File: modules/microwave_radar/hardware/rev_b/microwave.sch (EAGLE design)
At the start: 55 parts, among them J1 MODULE_GENERIC, J2 TC2030-JLINK-L, U1 SAM4LC8AA, U2 TLV62130, U3 MSGEQ7, U4 HB100, U5 OP284E_SEPARATE

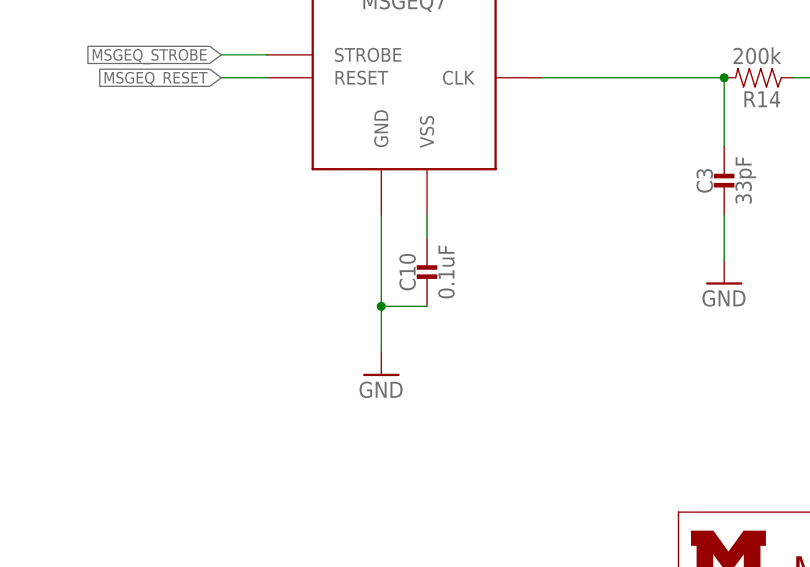
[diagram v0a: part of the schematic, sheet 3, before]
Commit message: Fix MSGEQ7 swapped pins!!!
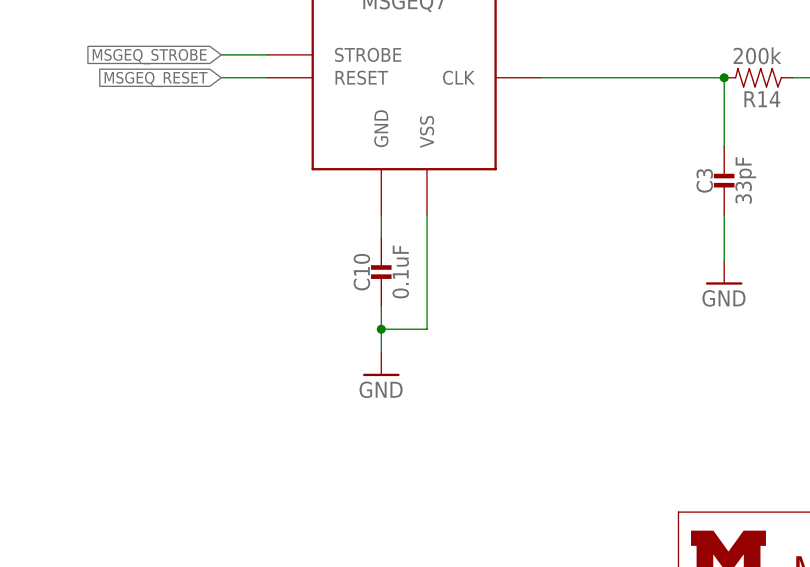
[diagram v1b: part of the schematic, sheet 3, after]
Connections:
- net GND: now also U3.VSS; no longer U3.GND
- net N$7: now also U3.GND; no longer U3.VSS
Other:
- moved on the sheet: C10
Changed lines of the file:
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@@
 <?xml version="1.0" encoding="utf-8"?>
 <!DOCTYPE eagle SYSTEM "eagle.dtd">
-<eagle version="7.7.0">
+<eagle version="6.6.0">
 <drawing>
 <settings>
@@
 <attribute name="DIGIKEY" x="86.36" y="91.44" size="1.778" layer="96" rot="R90" display="off"/>
 </instance>
-<instance part="C10" gate="G$1" x="99.06" y="38.1">
-<attribute name="DIGIKEY" x="99.06" y="38.1" size="1.778" layer="96" display="off"/>
+<instance part="C10" gate="G$1" x="93.98" y="38.1">
+<attribute name="DIGIKEY" x="93.98" y="38.1" size="1.778" layer="96" display="off"/>
 </instance>
 <instance part="C3" gate="G$1" x="132.08" y="48.26">
@@
 <segment>
 <pinref part="GND8" gate="1" pin="GND"/>
-<wire x1="99.06" y1="33.02" x2="93.98" y2="33.02" width="0.1524" layer="91"/>
-<wire x1="93.98" y1="33.02" x2="93.98" y2="27.94" width="0.1524" layer="91"/>
-<pinref part="U3" gate="G$1" pin="GND"/>
-<wire x1="93.98" y1="33.02" x2="93.98" y2="43.18" width="0.1524" layer="91"/>
-<junction x="93.98" y="33.02"/>
+<wire x1="93.98" y1="33.02" x2="93.98" y2="30.48" width="0.1524" layer="91"/>
 <pinref part="C10" gate="G$1" pin="2"/>
+<pinref part="U3" gate="G$1" pin="VSS"/>
+<wire x1="93.98" y1="30.48" x2="93.98" y2="27.94" width="0.1524" layer="91"/>
+<wire x1="99.06" y1="43.18" x2="99.06" y2="30.48" width="0.1524" layer="91"/>
+<wire x1="99.06" y1="30.48" x2="93.98" y2="30.48" width="0.1524" layer="91"/>
+<junction x="93.98" y="30.48"/>
 </segment>
 <segment>
@@
 </segment>
 </net>
-<net name="N$7" class="0">
-<segment>
-<pinref part="U3" gate="G$1" pin="VSS"/>
-<wire x1="99.06" y1="43.18" x2="99.06" y2="40.64" width="0.1524" layer="91"/>
-<pinref part="C10" gate="G$1" pin="1"/>
-</segment>
-</net>
 <net name="MSGEQ_OUT" class="0">
 <segment>
@@
 </segment>
 </net>
+<net name="N$7" class="0">
+<segment>
+<pinref part="U3" gate="G$1" pin="GND"/>
+<pinref part="C10" gate="G$1" pin="1"/>
+<wire x1="93.98" y1="40.64" x2="93.98" y2="43.18" width="0.1524" layer="91"/>
+</segment>
+</net>

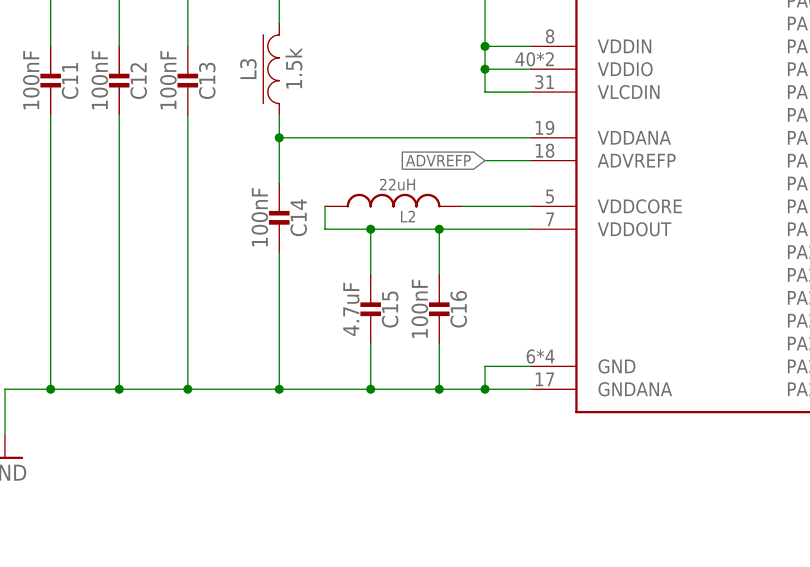
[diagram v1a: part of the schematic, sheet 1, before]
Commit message: moved caps
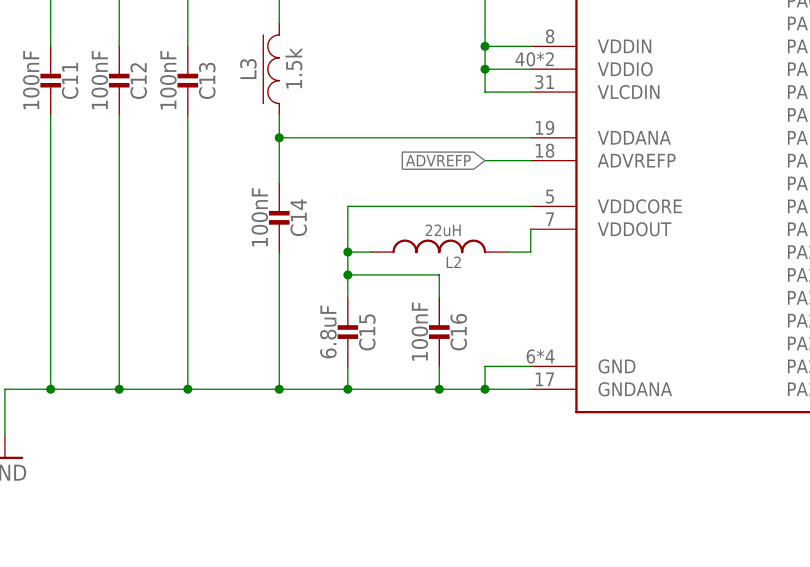
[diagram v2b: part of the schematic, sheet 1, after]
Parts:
- C15: value 4.7uF -> 6.8uF; device passives:CAPACITOR0402_CAP -> passives:CAPACITOR0603_CAP; DIGIKEY 490-13252-1-ND -> 445-7484-1-ND
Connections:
- removed net N$5: L2.2, U1.VDDCORE
- new net N$36: C15.2, C16.2, L2.1, U1.VDDCORE
- net N$6: now also L2.2; no longer C15.2, C16.2, L2.1
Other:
- moved on the sheet: C15, C16, L2

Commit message: added power gates, almost done routing
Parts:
- removed C21: 10uF, passives:CAPACITOR0805_CAP
- removed C22: 22uF, passives:CAPACITOR0603_CAP
- removed C7: 3.3nF, passives:CAPACITOR0402_CAP
- removed C8: 0.1uF, passives:CAPACITOR0402_CAP
- removed L1: 2.2uH, passives:INDUCTORIHL
- removed L3: 1.5k, passives:FERRITE_BEAD0402
- removed LED1: LED0603, leds:LED0603
- removed R1: 1k, passives:RESISTOR0402_RES
- removed R13: 100k, passives:RESISTOR0402_RES
- removed R15: 240k, passives:RESISTOR0402_RES
- removed R17: 750k, passives:RESISTOR0402_RES
- removed U2: TLV62130, chips:TLV62130
- added C28: 10 uF, passives:CAPACITOR0805_CAP
- added C29: 0.1 uF, passives:CAPACITOR0402_CAP
- added C30: 3.3 nF, passives:CAPACITOR0402_CAP
- added C31: 22 uF, passives:CAPACITOR0603_CAP
- added FB1: 1.5k, passives:FERRITE_BEAD0402
- added L5: 2.2 uH, passives:INDUCTORIHL
- added Q1, Q3: SI223DDS, fets:SI223DDS
- added R18, R22, R24: 100k, passives:RESISTOR0402_RES
- added R19, R23: 1k, passives:RESISTOR0402_RES
- added R20: 750k, passives:RESISTOR0402_RES
- added R21: 240k, passives:RESISTOR0402_RES
- added U7: TLV62130, chips:TLV62130
- J1: value MODULE_GENERIC -> MODULE_GENERIC_DEBUG; device signpost:MODULE_GENERIC -> signpost:MODULE_GENERIC_DEBUG
- R11, R12: value 100k -> 1M
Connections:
- net CONTROLLER_XIN renamed XIN
- net CONTROLLER_XOUT renamed XOUT
- removed net CONTROLLER_RESET: J2.!RESET, U1.!RESET
- removed net CONTROLLER_SWDCLK: J2.SWDCLK, R8.1, U1.TCK
- removed net CONTROLLER_SWDIO: J2.SWDIO, R7.1, U1.PA03
- removed net N$16: U1.PA06
- removed net N$20: L1.1, U2.SW
- removed net N$22: U1.PA11
- removed net N$23: R13.1, U2.PG
- removed net N$24: R15.2, R17.1, U2.FB
- removed net N$25: U1.PA12
- removed net N$4: LED1.ANODE, R1.2
- removed net N$8: C7.1, U2.SS/TR
- removed net USART2_RX: JP2.2, U1.PA25
- removed net USART2_TX: JP2.3, U1.PA26
- new net !RESET: J1.DBG_!RESET, J2.!RESET, U1.!RESET
- new net 3V3_GATED: C9.2, Q3.D, R10.2, R14.1, U3.VDD, U5G$2.VCC
- new net DBG_GPIO1: J1.DBG_GPIO1, U1.PA11
- new net DBG_GPIO2: J1.DBG_GPIO2, U1.PA12
- new net DBG_RX: J1.DBG_RX, JP2.2, U1.PA25
- new net DBG_TX: J1.DBG_TX, JP2.3, U1.PA26
- new net N$37: Q1.G, R18.1, R19.2
- new net N$38: Q3.G, R22.1, R23.2
- new net N$42: C30.2, U7.SS/TR
- new net N$43: L5.1, U7.SW
- new net N$44: R24.1, U7.PG
- new net N$45: R20.1, R21.2, U7.FB
- new net N$5: C17.2, Q1.D, U4.5V_1, U4.5V_2
- new net RADAR_POWER_GATE: R19.1, R23.1, U1.PA06
- new net SWDCLK: J1.DBG_SWDCLK, J2.SWDCLK, R8.1, U1.TCK
- new net SWDIO: J1.DBG_SWDIO, J2.SWDIO, R7.1, U1.PA03
- net +3V3: now also C31.2, FB1.P$2, L5.2, Q3.S, R20.2, R22.2, R24.2, U7.VOS; no longer C22.1, C9.2, L1.2, L3.P$2, R1.1, R10.2, R13.2, R14.1, R17.2, U2.VOS, U3.VDD, U5G$2.VCC
- net +5V: now also C28.1, C29.1, Q1.S, R18.2, U7.AVIN, U7.EN, U7.PVIN; no longer C17.2, C21.1, C8.1, U2.AVIN, U2.EN, U2.PVIN, U4.5V_1, U4.5V_2
- net GND: now also C28.2, C29.2, C30.1, C31.1, R21.1, U7.AGND, U7.DEF, U7.FSW, U7.PGND; no longer C21.2, C22.2, C7.2, C8.2, LED1.CATHODE, R15.1, U2.AGND, U2.DEF, U2.FSW, U2.PGND
- net N$13: now also FB1.P$1; no longer L3.P$1

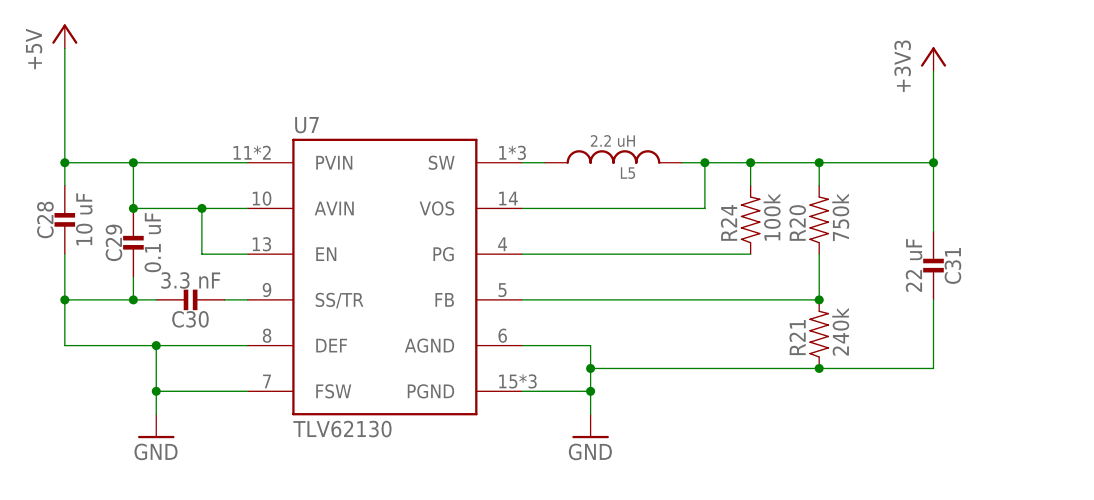
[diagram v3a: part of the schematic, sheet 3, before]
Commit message: changed values to not have space
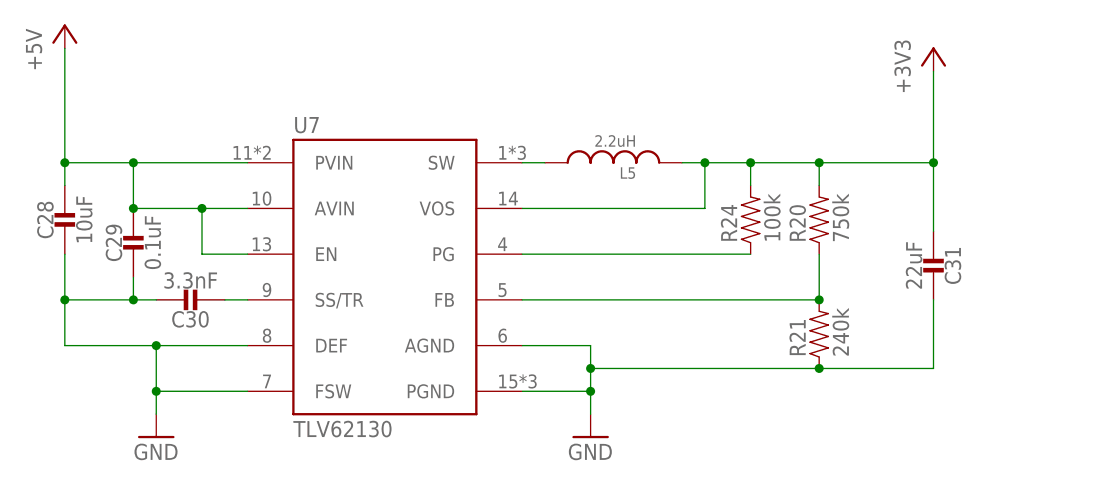
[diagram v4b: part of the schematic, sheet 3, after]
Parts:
- C28: value 10 uF -> 10uF
- C29: value 0.1 uF -> 0.1uF
- C30: value 3.3 nF -> 3.3nF
- C31: value 22 uF -> 22uF
- L5: value 2.2 uH -> 2.2uH
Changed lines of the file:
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@@
 <grid distance="0.1" unitdist="inch" unit="inch" style="lines" multiple="1" display="yes" altdistance="0.05" altunitdist="inch" altunit="inch"/>
 <layers>
-<layer number="1" name="Top" color="4" fill="1" visible="yes" active="no"/>
-<layer number="2" name="Route2" color="1" fill="3" visible="yes" active="no"/>
-<layer number="3" name="Route3" color="4" fill="3" visible="yes" active="no"/>
-<layer number="4" name="Route4" color="1" fill="4" visible="yes" active="no"/>
-<layer number="5" name="Route5" color="4" fill="4" visible="yes" active="no"/>
-<layer number="6" name="Route6" color="1" fill="8" visible="yes" active="no"/>
-<layer number="7" name="Route7" color="4" fill="8" visible="yes" active="no"/>
-<layer number="8" name="Route8" color="1" fill="2" visible="yes" active="no"/>
-<layer number="9" name="Route9" color="4" fill="2" visible="yes" active="no"/>
-<layer number="10" name="Route10" color="1" fill="7" visible="yes" active="no"/>
-<layer number="11" name="Route11" color="4" fill="7" visible="yes" active="no"/>
-<layer number="12" name="Route12" color="1" fill="5" visible="yes" active="no"/>
-<layer number="13" name="Route13" color="4" fill="5" visible="yes" active="no"/>
-<layer number="14" name="Route14" color="1" fill="6" visible="yes" active="no"/>
-<layer number="15" name="Route15" color="4" fill="6" visible="yes" active="no"/>
-<layer number="16" name="Bottom" color="1" fill="1" visible="yes" active="no"/>
-<layer number="17" name="Pads" color="2" fill="1" visible="yes" active="no"/>
-<layer number="18" name="Vias" color="2" fill="1" visible="yes" active="no"/>
-<layer number="19" name="Unrouted" color="6" fill="1" visible="yes" active="no"/>
-<layer number="20" name="Dimension" color="15" fill="1" visible="yes" active="no"/>
-<layer number="21" name="tPlace" color="7" fill="1" visible="yes" active="no"/>
-<layer number="22" name="bPlace" color="7" fill="1" visible="yes" active="no"/>
-<layer number="23" name="tOrigins" color="15" fill="1" visible="yes" active="no"/>
-<layer number="24" name="bOrigins" color="15" fill="1" visible="yes" active="no"/>
-<layer number="25" name="tNames" color="7" fill="1" visible="yes" active="no"/>
-<layer number="26" name="bNames" color="7" fill="1" visible="yes" active="no"/>
-<layer number="27" name="tValues" color="7" fill="1" visible="yes" active="no"/>
-<layer number="28" name="bValues" color="7" fill="1" visible="yes" active="no"/>
+<layer number="1" name="Top" color="4" fill="1" visible="no" active="no"/>
+<layer number="2" name="Route2" color="1" fill="3" visible="no" active="no"/>
+<layer number="3" name="Route3" color="4" fill="3" visible="no" active="no"/>
+<layer number="4" name="Route4" color="1" fill="4" visible="no" active="no"/>
+<layer number="5" name="Route5" color="4" fill="4" visible="no" active="no"/>
+<layer number="6" name="Route6" color="1" fill="8" visible="no" active="no"/>
+<layer number="7" name="Route7" color="4" fill="8" visible="no" active="no"/>
+<layer number="8" name="Route8" color="1" fill="2" visible="no" active="no"/>
+<layer number="9" name="Route9" color="4" fill="2" visible="no" active="no"/>
+<layer number="10" name="Route10" color="1" fill="7" visible="no" active="no"/>
+<layer number="11" name="Route11" color="4" fill="7" visible="no" active="no"/>
+<layer number="12" name="Route12" color="1" fill="5" visible="no" active="no"/>
+<layer number="13" name="Route13" color="4" fill="5" visible="no" active="no"/>
+<layer number="14" name="Route14" color="1" fill="6" visible="no" active="no"/>
+<layer number="15" name="Route15" color="4" fill="6" visible="no" active="no"/>
+<layer number="16" name="Bottom" color="1" fill="1" visible="no" active="no"/>
+<layer number="17" name="Pads" color="2" fill="1" visible="no" active="no"/>
+<layer number="18" name="Vias" color="2" fill="1" visible="no" active="no"/>
+<layer number="19" name="Unrouted" color="6" fill="1" visible="no" active="no"/>
+<layer number="20" name="Dimension" color="15" fill="1" visible="no" active="no"/>
+<layer number="21" name="tPlace" color="7" fill="1" visible="no" active="no"/>
+<layer number="22" name="bPlace" color="7" fill="1" visible="no" active="no"/>
+<layer number="23" name="tOrigins" color="15" fill="1" visible="no" active="no"/>
+<layer number="24" name="bOrigins" color="15" fill="1" visible="no" active="no"/>
+<layer number="25" name="tNames" color="7" fill="1" visible="no" active="no"/>
+<layer number="26" name="bNames" color="7" fill="1" visible="no" active="no"/>
+<layer number="27" name="tValues" color="7" fill="1" visible="no" active="no"/>
+<layer number="28" name="bValues" color="7" fill="1" visible="no" active="no"/>
 <layer number="29" name="tStop" color="7" fill="3" visible="no" active="no"/>
 <layer number="30" name="bStop" color="7" fill="6" visible="no" active="no"/>
@@
 <layer number="35" name="tGlue" color="7" fill="4" visible="no" active="no"/>
 <layer number="36" name="bGlue" color="7" fill="5" visible="no" active="no"/>
-<layer number="37" name="tTest" color="7" fill="1" visible="yes" active="no"/>
-<layer number="38" name="bTest" color="7" fill="1" visible="yes" active="no"/>
+<layer number="37" name="tTest" color="7" fill="1" visible="no" active="no"/>
+<layer number="38" name="bTest" color="7" fill="1" visible="no" active="no"/>
 <layer number="39" name="tKeepout" color="4" fill="11" visible="no" active="no"/>
 <layer number="40" name="bKeepout" color="1" fill="11" visible="no" active="no"/>
@@
 <layer number="44" name="Drills" color="7" fill="1" visible="no" active="no"/>
 <layer number="45" name="Holes" color="7" fill="1" visible="no" active="no"/>
-<layer number="46" name="Milling" color="3" fill="1" visible="yes" active="no"/>
-<layer number="47" name="Measures" color="7" fill="1" visible="yes" active="no"/>
-<layer number="48" name="Document" color="7" fill="1" visible="yes" active="no"/>
-<layer number="49" name="Reference" color="7" fill="1" visible="yes" active="no"/>
-<layer number="50" name="dxf" color="7" fill="1" visible="yes" active="no"/>
-<layer number="51" name="tDocu" color="7" fill="1" visible="yes" active="no"/>
-<layer number="52" name="bDocu" color="7" fill="1" visible="yes" active="no"/>
-<layer number="53" name="tGND_GNDA" color="7" fill="9" visible="yes" active="no"/>
-<layer number="54" name="bGND_GNDA" color="1" fill="9" visible="yes" active="no"/>
-<layer number="56" name="wert" color="7" fill="1" visible="yes" active="no"/>
-<layer number="57" name="tCAD" color="7" fill="1" visible="yes" active="no"/>
-<layer number="59" name="Invisible" color="7" fill="1" visible="yes" active="no"/>
+<layer number="46" name="Milling" color="3" fill="1" visible="no" active="no"/>
+<layer number="47" name="Measures" color="7" fill="1" visible="no" active="no"/>
+<layer number="48" name="Document" color="7" fill="1" visible="no" active="no"/>
+<layer number="49" name="Reference" color="7" fill="1" visible="no" active="no"/>
+<layer number="50" name="dxf" color="7" fill="1" visible="no" active="no"/>
+<layer number="51" name="tDocu" color="7" fill="1" visible="no" active="no"/>
+<layer number="52" name="bDocu" color="7" fill="1" visible="no" active="no"/>
+<layer number="53" name="tGND_GNDA" color="7" fill="9" visible="no" active="no"/>
+<layer number="54" name="bGND_GNDA" color="1" fill="9" visible="no" active="no"/>
+<layer number="56" name="wert" color="7" fill="1" visible="no" active="no"/>
+<layer number="57" name="tCAD" color="7" fill="1" visible="no" active="no"/>
+<layer number="59" name="Invisible" color="7" fill="1" visible="no" active="no"/>
 <layer number="60" name="bCarbon" color="7" fill="1" visible="no" active="no"/>
-<layer number="61" name="stand" color="7" fill="1" visible="yes" active="no"/>
+<layer number="61" name="stand" color="7" fill="1" visible="no" active="no"/>
 <layer number="90" name="Modules" color="5" fill="1" visible="yes" active="yes"/>
 <layer number="91" name="Nets" color="2" fill="1" visible="yes" active="yes"/>
@@
 </part>
 <part name="U7" library="chips" deviceset="TLV62130" device=""/>
-<part name="C28" library="passives" deviceset="CAPACITOR" device="0805_CAP" value="10 uF"/>
-<part name="C29" library="passives" deviceset="CAPACITOR" device="0402_CAP" value="0.1 uF"/>
-<part name="C30" library="passives" deviceset="CAPACITOR" device="0402_CAP" value="3.3 nF"/>
-<part name="C31" library="passives" deviceset="CAPACITOR" device="0603_CAP" value="22 uF"/>
+<part name="C28" library="passives" deviceset="CAPACITOR" device="0805_CAP" value="10uF"/>
+<part name="C29" library="passives" deviceset="CAPACITOR" device="0402_CAP" value="0.1uF"/>
+<part name="C30" library="passives" deviceset="CAPACITOR" device="0402_CAP" value="3.3nF"/>
+<part name="C31" library="passives" deviceset="CAPACITOR" device="0603_CAP" value="22uF"/>
 <part name="R20" library="passives" deviceset="RESISTOR" device="0402_RES" value="750k">
 <attribute name="DIGIKEY" value="P750KLCT-ND"/>
@@
 </part>
 <part name="R24" library="passives" deviceset="RESISTOR" device="0402_RES" value="100k"/>
-<part name="L5" library="passives" deviceset="INDUCTOR" device="IHL" value="2.2 uH"/>
+<part name="L5" library="passives" deviceset="INDUCTOR" device="IHL" value="2.2uH"/>
 <part name="GND13" library="umich" deviceset="GND" device=""/>
 <part name="GND14" library="umich" deviceset="GND" device=""/>
